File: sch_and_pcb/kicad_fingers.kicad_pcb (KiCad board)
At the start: 2 copper layers, 109.8 x 90.3 mm, 74 parts, among them J1 EP_BOT, J2 EP_TOP, J3 AUX, J4 AUX, J5 SJ-43514, J6 THM_TOP, J7 THM_BOT, J8 ALTLED, J9 ALTLED, M3_Mounting_Hole VAL**, P1 TST, P10 TST, P11 TST, P12 TST, P13 TST, P2 TST, P3 TST, P4 TST, P5 TST, P6 TST, P7 TST, P8 TST, P9 TST, Q1 PNP_KSA1298, SW1 SPST, U1 TEENSY2P0, U2 LIN_REG, U3 PCA9306, U4 PCA9655E, X1 RF5S, X2 RF5S, X3 RF5S, X4 RF5S

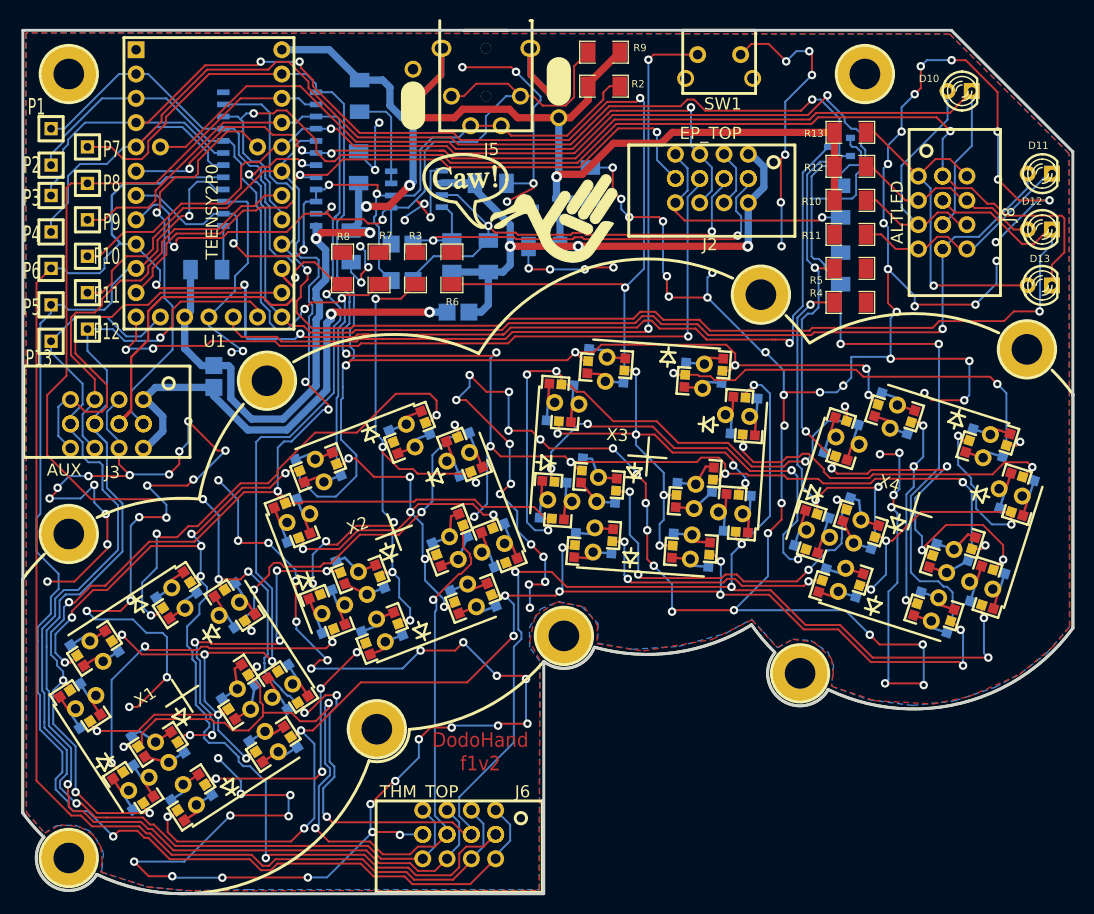
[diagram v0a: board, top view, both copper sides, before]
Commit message: Changed the resistor pads to the same solder bridges as the thumb unit. Changed the footprint on the board and fixed the tracks.
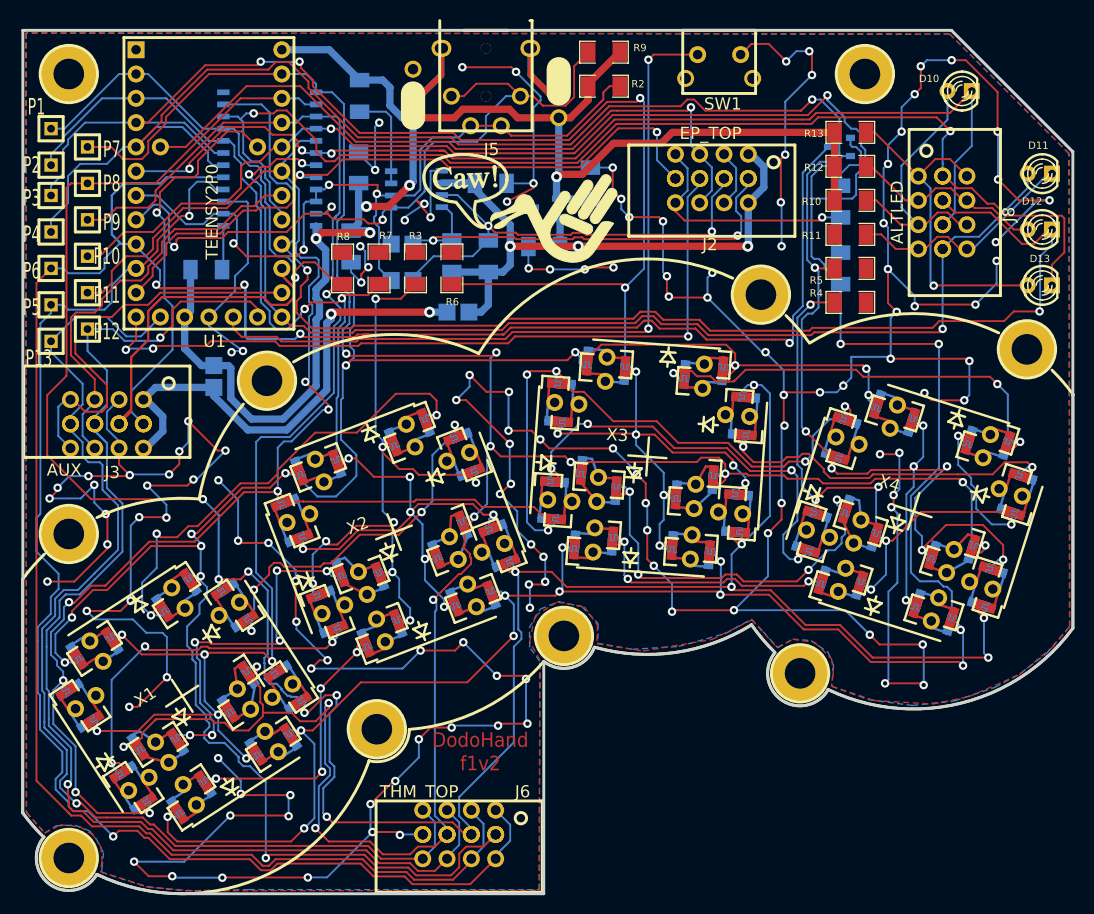
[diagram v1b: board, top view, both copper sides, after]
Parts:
- X1, X2, X3, X4: footprint rf5s -> footprints:rf5s
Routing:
- net /ROW4: track 237.1 -> 234.1 mm
- net /ROW1: track 269.9 -> 271.7 mm
- net /COL0: track 155.3 -> 153.9 mm
- net Net-(X3-Pad2): track 46.5 -> 47.7 mm
- net /COL2: track 189.6 -> 190.7 mm
- net /ROW2: track 263.9 -> 262.8 mm
- net /ROW0: track 266.1 -> 265.3 mm
- net Net-(X3-Pad8): track 29.3 -> 30.0 mm
- net /COL3: track 223.6 -> 223.0 mm
- net Net-(X3-Pad4): track 39.2 -> 39.8 mm

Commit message: Increased the gaps to 6mil
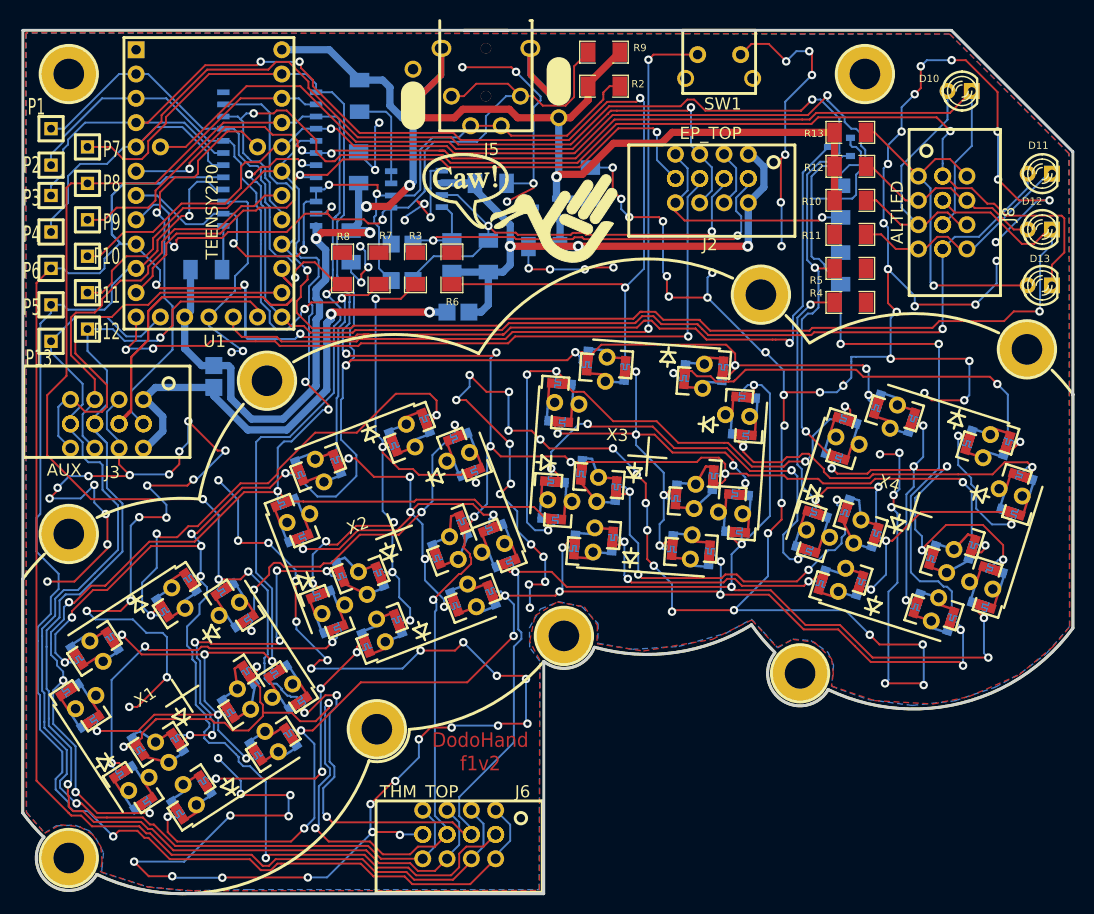
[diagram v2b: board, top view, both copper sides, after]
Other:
- rule trace_min: 0.2032 -> 0.1524
